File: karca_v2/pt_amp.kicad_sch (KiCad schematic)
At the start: 41 parts, among them J5 Screw_Terminal_01x08, U4 TLV9304xD, U5 TLV9304xD, U6 MCP3208

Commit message: modified sch
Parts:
- C11, C13, C15, C8: value 1n -> 0.075u
- C12, C14, C7, C9: value 1n -> 0.15u
- R11, R12, R16, R17, R21, R22, R6, R7: value 68k -> 1k

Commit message: updated
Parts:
- added C59, C60: 10u, Capacitor_SMD:C_1206_3216Metric, symbol Device:C
- added R111: 10.4M, symbol Device:R_US
- added R112: 1.2M, symbol Device:R_US
- added U42: TPS7A24, symbol karca_lib:TPS7A24
- renumbered C9 to Ce
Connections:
- net +12V: now also C59.1, C60.1, R111.1, U42.1 (IN), U42.3 (EN), U42.5 (OUT)
- net GND: now also C59.2, C60.2, R112.2, U42.2 (GND)
- new net: R111.2, R112.1, U42.4 (FB)
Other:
- note added: "R111+ R112 <12M"
- note added: "R111/R112 = 8.68"
- note added: "Regulated 12V"
- note added: "Unregulated 12V"
- note added: "fc = 1.5kHz"
- moved on the sheet: TP5, U4E, U5E

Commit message: Version alpha
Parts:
- removed C11, C13, C15, C8: 0.075u, Capacitor_SMD:C_1206_3216Metric, symbol Device:C
- removed C12, C14, C7, Ce: 0.15u, Capacitor_SMD:C_1206_3216Metric, symbol Device:C
- removed D10, D11, D8, D9: D_Schottky, Diode_SMD:D_SMA, symbol Device:D_Schottky
- removed R10, R15, R20, R25: 6.7k, symbol Device:R_US
- removed R11, R12, R16, R17, R21, R22, R6, R7: 1k, symbol Device:R_US
- removed R13, R18, R23, R8: 30, symbol Device:R_US
- removed R14, R19, R24, R9: 47k, symbol Device:R_US
- removed TP5, TP6, TP7, TP8: TestPoint, symbol Connector:TestPoint
- removed U4: TLV9304xD, Package_SO:SO-14_3.9x8.65mm_P1.27mm, symbol Amplifier_Operational:TLV9304xD
- removed unit 4 of U5
- removed unit 3 of U5
- removed unit 1 of U5
- removed unit 2 of U5
- added C62, C63, C64, C65: 100n, Capacitor_SMD:C_1206_3216Metric, symbol Device:C
- added TP10, TP11, TP12, TP13: TestPoint, TestPoint:TestPoint_Pad_D2.0mm, symbol Connector:TestPoint
- added U10: NUP4202, Package_TO_SOT_SMD:SOT-363_SC-70-6, symbol Power_Protection:NUP4202
- added U7: TLV9304xD, Package_SO:SO-14_3.9x8.65mm_P1.27mm, symbol Amplifier_Operational:TLV9304xD
- J6: renamed from J5; footprint (none) -> terminal blocks:P-2604-1108
- R6: renamed from R111; footprint (none) -> Resistor_SMD:R_1206_3216Metric
- R7: renamed from R112; footprint (none) -> Resistor_SMD:R_1206_3216Metric
- U6: renamed from U42; footprint (none) -> Package_TO_SOT_SMD:SOT-23-5
- U9: renamed from U6; footprint (none) -> Package_SO:SOIC-16_3.9x9.9mm_P1.27mm
- renumbered C60 to C3, C59 to C4, C10 to C5, U5 to U8
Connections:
- net +12V: no longer C3.1, J6.1 (Pin_1), J6.3 (Pin_3), J6.5 (Pin_5), J6.7 (Pin_7), R6.1, U6.5 (OUT)
- net +5V: now also C62.2, C63.1, U10.5, U7.4 (V+)
- net GND: now also C62.1, C63.2, C64.1, C64.2, C65.1, C65.2, U10.2, U7.11 (V-)
- net pt_circuitry/IN: now reaches J6.2 (Pin_2)
- net pt_circuitry1/OUT: now reaches U9.2 (CH1)
- net pt_circuitry1/OUT: now also TP11.1, U10.4
- net pt_circuitry3/OUT: now reaches U9.4 (CH3)
- net pt_circuitry3/OUT: now also TP13.1, U10.1
- net pt_circuitry3/IN: now reaches J6.8 (Pin_8)
- net pt_circuitry/OUT: now reaches U9.1 (CH0)
- net pt_circuitry/OUT: now also TP10.1, U10.6
- net pt_circuitry2/OUT: now reaches U9.3 (CH2)
- net pt_circuitry2/OUT: now also TP12.1, U10.3
- net pt_circuitry2/IN: now reaches J6.6 (Pin_6)
- net pt_circuitry1/IN: now reaches J6.4 (Pin_4)
- new net: C3.1, J6.1 (Pin_1), J6.3 (Pin_3), J6.5 (Pin_5), J6.7 (Pin_7), R6.1, U6.5 (OUT)
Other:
- added sheet pt_circuitry (pt_circuitry.kicad_sch)
- added sheet pt_circuitry1 (pt_circuitry.kicad_sch)
- added sheet pt_circuitry2 (pt_circuitry.kicad_sch)
- added sheet pt_circuitry3 (pt_circuitry.kicad_sch)
- note removed: "Gain = 8"
- note removed: "Internal protection circuitry (no need for protection diodes)"
- note removed: "Rail-to-rail op-amp Slew rate: 3V/us(0.5V/us for LM324)"
- note removed: "Resolution = 0.31psi"
- note removed: "buffer to prevent current leak into op-amp"
- note removed: "fc = 1.5kHz"
- moved on the sheet: C3, C4, C5, J6, R6, R7, U6, U8E, U9

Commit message: fkkkkkkkkkk
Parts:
- renumbered U10 to U12
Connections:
- net TC_1_ADC is gone; now on net pt_circuitry2/OUT: U9.5 (CH4)
- net TC_2_ADC is gone; now on net pt_circuitry3/OUT: U9.6 (CH5)
- net TC_3_ADC is gone; now on net pt_circuitry/OUT: U9.7 (CH6)
- net TC_4_ADC is gone; now on net pt_circuitry1/OUT: U9.8 (CH7)
- net pt_circuitry/OUT: now also U12.1; no longer U12.6, U9.1 (CH0)
- net pt_circuitry1/OUT: now also U12.3; no longer U12.4, U9.2 (CH1)
- net pt_circuitry2/OUT: now also U12.4; no longer U12.3, U9.3 (CH2)
- net pt_circuitry3/OUT: now also U12.6; no longer U12.1, U9.4 (CH3)
- new net DRV1_ADC: U9.3 (CH2)
- new net DRV2_ADC: U9.2 (CH1)
- new net DRV3_ADC: U9.1 (CH0)
- new net DRV4_ADC: U9.4 (CH3)
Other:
- moved on the sheet: C5, TP10, TP11, U12, U9

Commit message: discrete traces
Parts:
- renumbered C3 to C10, C4 to C11, C64 to C12, C65 to C13, C5 to C14, C62 to C8, C63 to C9, U12 to U10

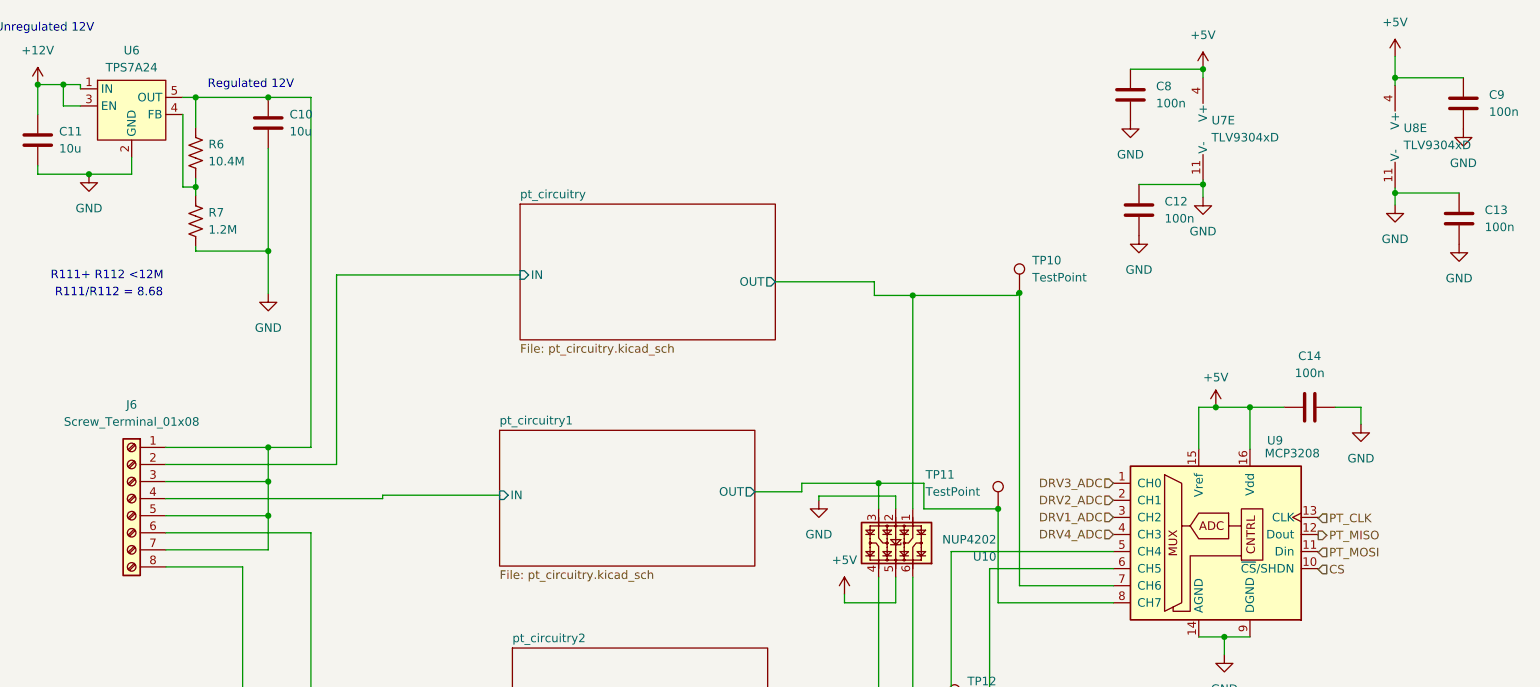
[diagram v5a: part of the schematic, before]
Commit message: fixed TVS Diodes
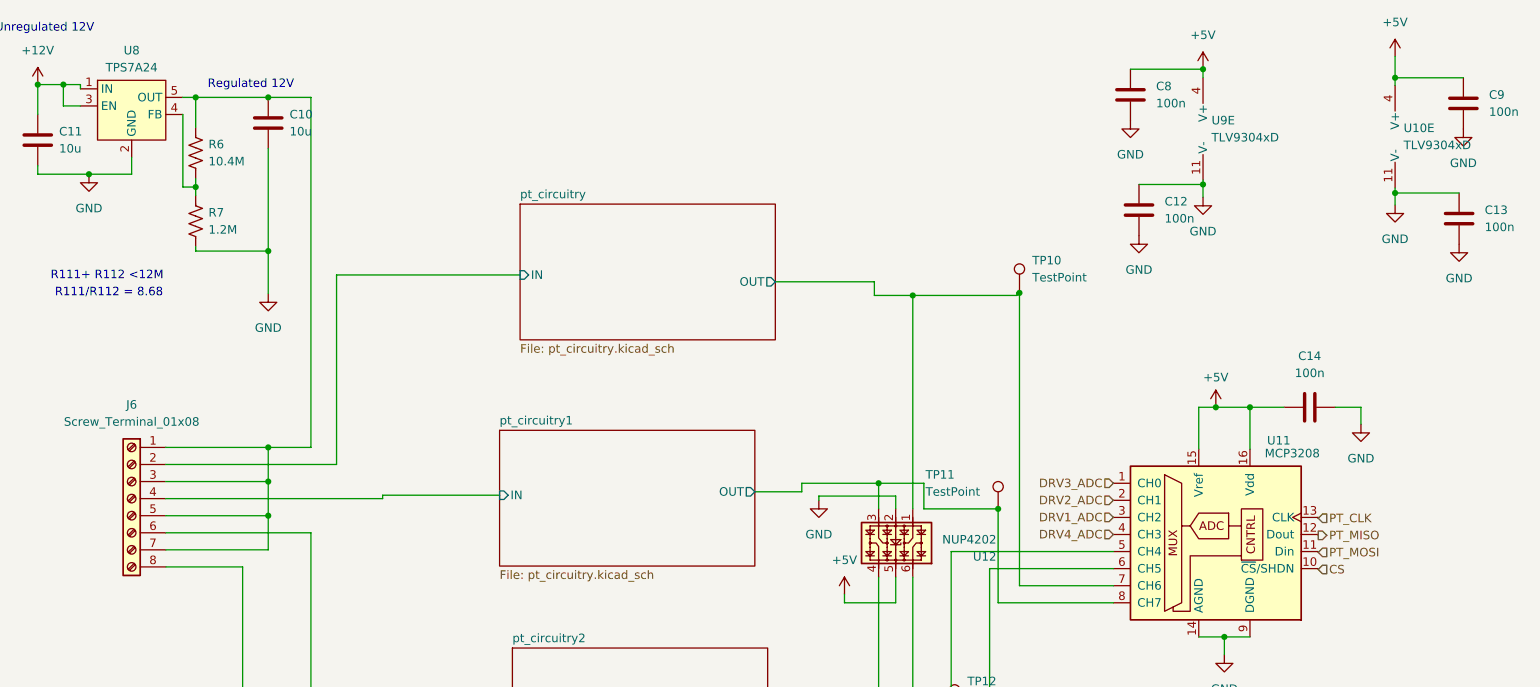
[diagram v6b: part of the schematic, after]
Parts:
- renumbered U8 to U10, U9 to U11, U10 to U12, U6 to U8, U7 to U9
